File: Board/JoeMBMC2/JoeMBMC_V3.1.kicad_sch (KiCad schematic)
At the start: 69 parts, among them J1 5007620481, J2 CAN2_T, J3 CAN1_T, Q1 BSO615NG, Q2 BSO615NG, Q3 P-Chanel Mosfet, U1 Teensy4.0, U2 SN65HVD230, U3 DCDC 5V, U4 IS281-4, U5 SN65HVD230, U6 DCDC 3.3V, U7 Level Shifter 5V to 3V, U8 Level Shifter 5V to 3V

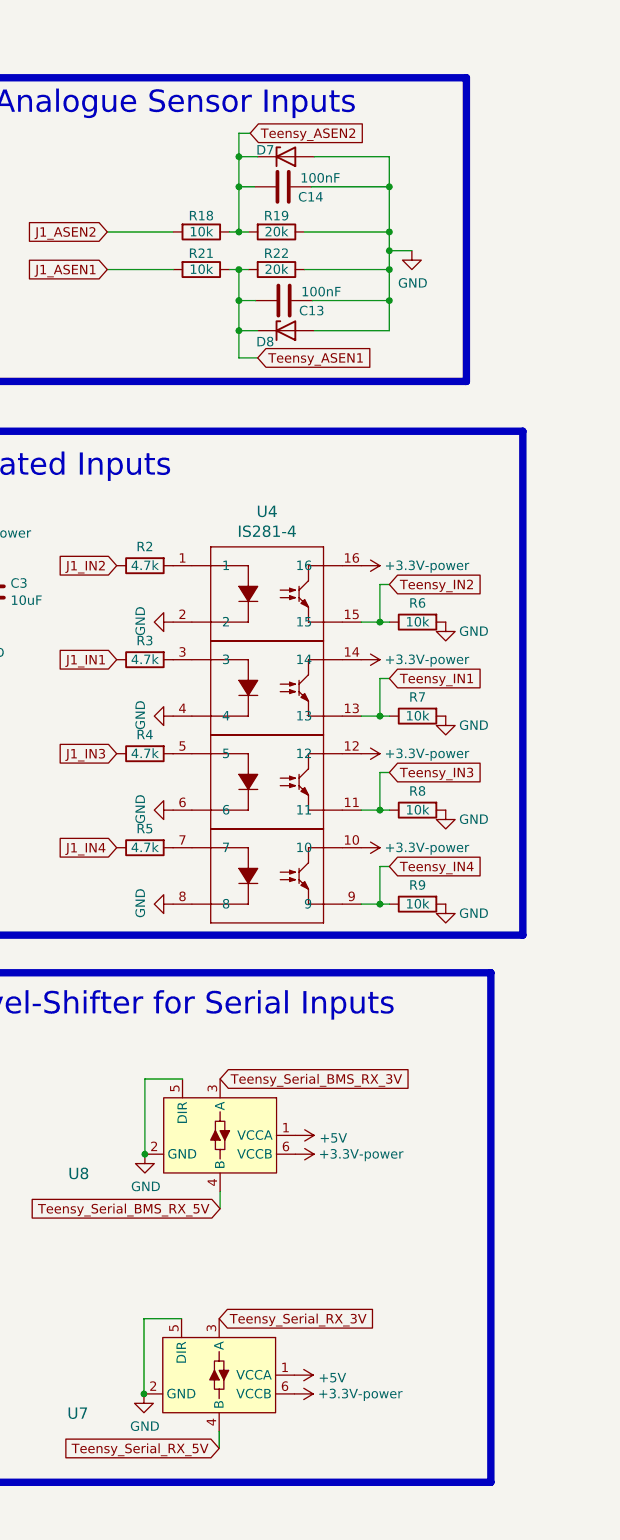
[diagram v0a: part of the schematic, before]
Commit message: remove zener on analogue sensor inputs
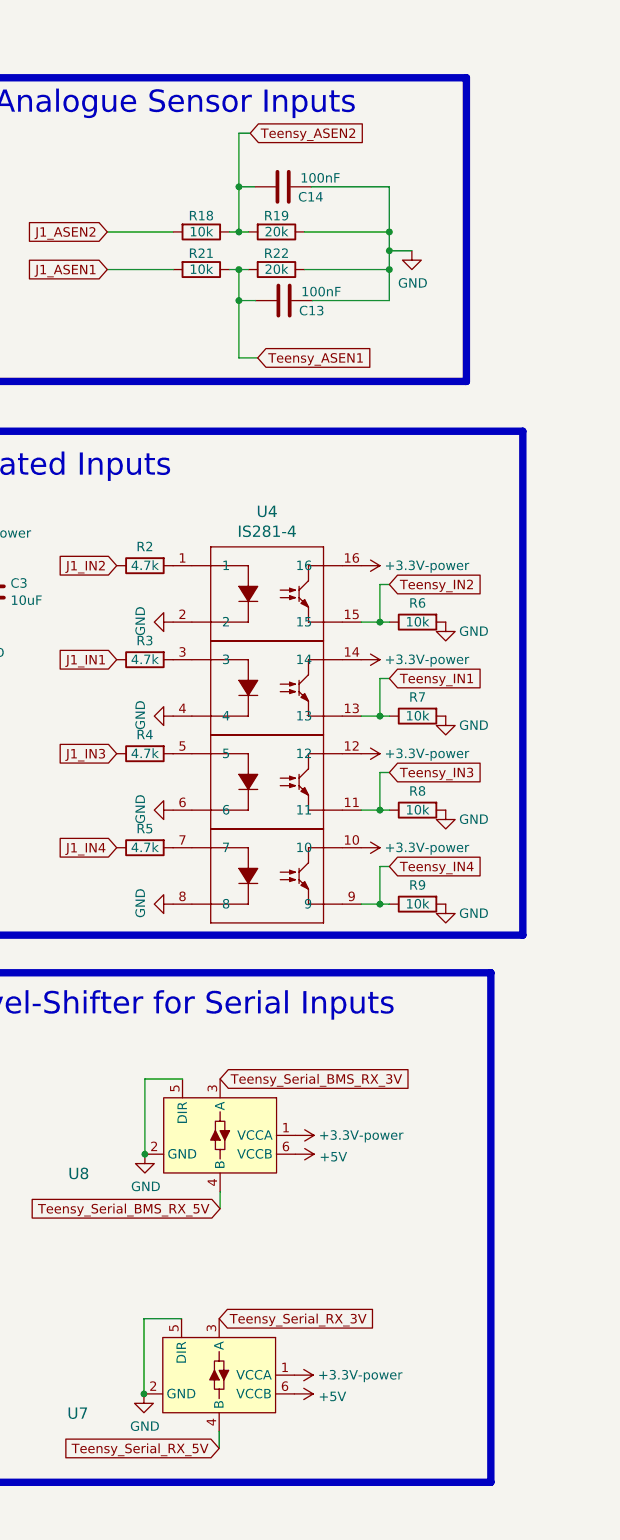
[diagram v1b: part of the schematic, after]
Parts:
- removed D7, D8: D_Zener, Diode_SMD:D_SOD-123, symbol Device:D_Zener
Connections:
- net +3V3: now also U7.1 (VCCA), U8.1 (VCCA); no longer U7.6 (VCCB), U8.6 (VCCB)
- net +5V: now also U7.6 (VCCB), U8.6 (VCCB); no longer U7.1 (VCCA), U8.1 (VCCA)
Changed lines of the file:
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@@
   (junction (at 51.562 69.85) (diameter 0) (color 0 0 0 0)
   )
-  (junction (at 376.301 87.122) (diameter 0) (color 0 0 0 0)
-  )
   (junction (at 355.981 82.931) (diameter 0) (color 0 0 0 0)
   )
@@
   (junction (at 343.154 234.823) (diameter 0) (color 0 0 0 0)
   )
-  (junction (at 355.981 91.186) (diameter 0) (color 0 0 0 0)
-  )
   (junction (at 224.79 253.238) (diameter 0) (color 0 0 0 0)
   )
@@
   (junction (at 68.072 40.64) (diameter 0) (color 0 0 0 0)
   )
-  (junction (at 376.301 71.755) (diameter 0) (color 0 0 0 0)
-  )
   (junction (at 376.301 80.391) (diameter 0) (color 0 0 0 0)
   )
@@
   (junction (at 375.031 143.256) (diameter 0) (color 0 0 0 0)
   )
-  (junction (at 355.981 67.691) (diameter 0) (color 0 0 0 0)
-  )
   (junction (at 81.153 137.16) (diameter 0) (color 0 0 0 0)
   )
@@
     (stroke (width 0) (type default))
   )
-  (wire (pts (xy 355.981 67.691) (xy 358.521 67.691))
-    (stroke (width 0) (type default))
-  )
   (wire (pts (xy 188.341 205.867) (xy 188.849 205.867))
     (stroke (width 0) (type default))
@@
     (stroke (width 0) (type default))
   )
-  (wire (pts (xy 355.981 91.186) (xy 358.521 91.186))
-    (stroke (width 0) (type default))
-  )
   (wire (pts (xy 59.563 144.78) (xy 60.833 144.78))
     (stroke (width 0) (type default))
@@
     (stroke (width 0) (type default))
   )
-  (wire (pts (xy 355.981 87.122) (xy 355.981 91.186))
-    (stroke (width 0) (type default))
-  )
   (wire (pts (xy 68.072 52.07) (xy 68.072 55.88))
     (stroke (width 0) (type default))
   )
-  (wire (pts (xy 376.301 87.122) (xy 376.301 91.186))
-    (stroke (width 0) (type default))
-  )
   (wire (pts (xy 234.95 263.398) (xy 247.65 263.398))
     (stroke (width 0) (type default))
@@
     (stroke (width 0) (type default))
   )
-  (wire (pts (xy 366.141 67.691) (xy 376.301 67.691))
-    (stroke (width 0) (type default))
-  )
   (wire (pts (xy 60.833 137.16) (xy 58.293 137.16))
     (stroke (width 0) (type default))
@@
     (stroke (width 0) (type default))
   )
-  (wire (pts (xy 376.301 67.691) (xy 376.301 71.755))
-    (stroke (width 0) (type default))
-  )
   (wire (pts (xy 50.292 69.85) (xy 51.562 69.85))
     (stroke (width 0) (type default))
@@
     (stroke (width 0) (type default))
   )
-  (wire (pts (xy 355.981 67.691) (xy 355.981 64.516))
-    (stroke (width 0) (type default))
-  )
   (wire (pts (xy 365.76 71.755) (xy 376.301 71.755))
     (stroke (width 0) (type default))
@@
     (stroke (width 0) (type default))
   )
-  (wire (pts (xy 366.141 91.186) (xy 376.301 91.186))
-    (stroke (width 0) (type default))
-  )
   (wire (pts (xy 248.92 206.375) (xy 246.38 206.375))
     (stroke (width 0) (type default))
@@
     (stroke (width 0) (type default))
   )
-  (wire (pts (xy 355.981 91.186) (xy 355.981 94.869))
+  (wire (pts (xy 355.981 87.122) (xy 355.981 94.869))
     (stroke (width 0) (type default))
   )
@@
     (stroke (width 0) (type default))
   )
-  (wire (pts (xy 355.981 67.691) (xy 355.981 71.755))
+  (wire (pts (xy 355.981 64.516) (xy 355.981 71.755))
     (stroke (width 0) (type default))
   )
@@
     )
   )
-  (symbol (lib_id "Device:D_Zener") (at 362.331 91.186 0) (unit 1)
-    (in_bom yes) (on_board yes) (dnp no)
-    (property "Reference" "D8" (at 359.537 92.71 0)
-      (effects (font (size 1.27 1.27)))
-    )
-    (property "Value" "D_Zener" (at 367.665 92.583 0)
-      (effects (font (size 1.27 1.27)) hide)
-    )
-    (property "Footprint" "Diode_SMD:D_SOD-123" (at 362.331 91.186 0)
-      (effects (font (size 1.27 1.27)) hide)
-    )
-    (property "Datasheet" "~" (at 362.331 91.186 0)
-      (effects (font (size 1.27 1.27)) hide)
-    )
-    (property "LCSC" "C2891770" (at 362.331 91.186 0)
-      (effects (font (size 1.27 1.27)) hide)
-    )
-    (pin "2")
-    (pin "1")
-    (instances
-      (project "JoeMBMC_V3.1"
-        (path "/8ca989a6-8473-46db-aafb-d17085f293f9"
-          (reference "D8") (unit 1)
-        )
-      )
-    )
-  )
   (symbol (lib_id "Connector:Conn_01x02_Pin") (at 210.82 201.295 0) (unit 1)
     (in_bom yes) (on_board yes) (dnp no)
@@
     )
   )
-  (symbol (lib_id "Device:D_Zener") (at 362.331 67.691 0) (unit 1)
-    (in_bom yes) (on_board yes) (dnp no)
-    (property "Reference" "D7" (at 359.537 66.802 0)
-      (effects (font (size 1.27 1.27)))
-    )
-    (property "Value" "D_Zener" (at 367.665 69.088 0)
-      (effects (font (size 1.27 1.27)) hide)
-    )
-    (property "Footprint" "Diode_SMD:D_SOD-123" (at 362.331 67.691 0)
-      (effects (font (size 1.27 1.27)) hide)
-    )
-    (property "Datasheet" "~" (at 362.331 67.691 0)
-      (effects (font (size 1.27 1.27)) hide)
-    )
-    (property "LCSC" "C2891770" (at 362.331 67.691 0)
-      (effects (font (size 1.27 1.27)) hide)
-    )
-    (pin "2")
-    (pin "1")
-    (instances
-      (project "JoeMBMC_V3.1"
-        (path "/8ca989a6-8473-46db-aafb-d17085f293f9"
-          (reference "D7") (unit 1)
-        )
-      )
-    )
-  )
   (symbol (lib_id "power:GND") (at 275.463 44.069 0) (unit 1)
     (in_bom yes) (on_board yes) (dnp no)
@@
     )
   )
-  (symbol (lib_id "power:+5V") (at 363.474 232.283 270) (unit 1)
+  (symbol (lib_id "power:+5V") (at 363.474 234.823 270) (unit 1)
     (in_bom yes) (on_board yes) (dnp no)
-    (property "Reference" "#PWR028" (at 359.664 232.283 0)
+    (property "Reference" "#PWR028" (at 359.664 234.823 0)
       (effects (font (size 1.27 1.27)) hide)
     )
-    (property "Value" "+5V" (at 366.7252 232.664 90)
+    (property "Value" "+5V" (at 366.7252 235.204 90)
       (effects (font (size 1.27 1.27)) (justify left))
     )
-    (property "Footprint" "" (at 363.474 232.283 0)
+    (property "Footprint" "" (at 363.474 234.823 0)
       (effects (font (size 1.27 1.27)) hide)
     )
-    (property "Datasheet" "" (at 363.474 232.283 0)
+    (property "Datasheet" "" (at 363.474 234.823 0)
       (effects (font (size 1.27 1.27)) hide)
     )
@@
     )
   )
-  (symbol (lib_id "JoeMBMS_V2.0-rescue:+3.3V-power") (at 363.474 234.823 270) (unit 1)
+  (symbol (lib_id "JoeMBMS_V2.0-rescue:+3.3V-power") (at 363.474 232.283 270) (unit 1)
     (in_bom yes) (on_board yes) (dnp no)
-    (property "Reference" "#PWR029" (at 359.664 234.823 0)
+    (property "Reference" "#PWR029" (at 359.664 232.283 0)
       (effects (font (size 1.27 1.27)) hide)
     )
-    (property "Value" "+3.3V-power" (at 366.6489 234.823 90)
+    (property "Value" "+3.3V-power" (at 366.6489 232.283 90)
       (effects (font (size 1.27 1.27)) (justify left))
     )
-    (property "Footprint" "" (at 363.474 234.823 0)
+    (property "Footprint" "" (at 363.474 232.283 0)
       (effects (font (size 1.27 1.27)) hide)
     )
-    (property "Datasheet" "" (at 363.474 234.823 0)
+    (property "Datasheet" "" (at 363.474 232.283 0)
       (effects (font (size 1.27 1.27)) hide)
     )
@@
     )
   )
-  (symbol (lib_id "power:+5V") (at 363.601 199.898 270) (unit 1)
+  (symbol (lib_id "power:+5V") (at 363.601 202.438 270) (unit 1)
     (in_bom yes) (on_board yes) (dnp no)
-    (property "Reference" "#PWR034" (at 359.791 199.898 0)
+    (property "Reference" "#PWR034" (at 359.791 202.438 0)
       (effects (font (size 1.27 1.27)) hide)
     )
-    (property "Value" "+5V" (at 366.8522 200.279 90)
+    (property "Value" "+5V" (at 366.8522 202.819 90)
       (effects (font (size 1.27 1.27)) (justify left))
     )
-    (property "Footprint" "" (at 363.601 199.898 0)
+    (property "Footprint" "" (at 363.601 202.438 0)
       (effects (font (size 1.27 1.27)) hide)
     )
-    (property "Datasheet" "" (at 363.601 199.898 0)
+    (property "Datasheet" "" (at 363.601 202.438 0)
       (effects (font (size 1.27 1.27)) hide)
     )
@@
     )
   )
-  (symbol (lib_id "JoeMBMS_V2.0-rescue:+3.3V-power") (at 363.601 202.438 270) (unit 1)
+  (symbol (lib_id "JoeMBMS_V2.0-rescue:+3.3V-power") (at 363.601 199.898 270) (unit 1)
     (in_bom yes) (on_board yes) (dnp no)
-    (property "Reference" "#PWR035" (at 359.791 202.438 0)
+    (property "Reference" "#PWR035" (at 359.791 199.898 0)
       (effects (font (size 1.27 1.27)) hide)
     )
-    (property "Value" "+3.3V-power" (at 366.7759 202.438 90)
+    (property "Value" "+3.3V-power" (at 366.7759 199.898 90)
       (effects (font (size 1.27 1.27)) (justify left))
     )
-    (property "Footprint" "" (at 363.601 202.438 0)
+    (property "Footprint" "" (at 363.601 199.898 0)
       (effects (font (size 1.27 1.27)) hide)
     )
-    (property "Datasheet" "" (at 363.601 202.438 0)
+    (property "Datasheet" "" (at 363.601 199.898 0)
       (effects (font (size 1.27 1.27)) hide)
     )

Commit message: USB-Flex-Board
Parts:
- D1, D2, D3, D4: LCSC C37049 -> C8598
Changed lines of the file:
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@@
       (effects (font (size 1.27 1.27)) hide)
     )
-    (property "LCSC" "C37049" (at 71.882 91.44 0)
+    (property "LCSC" "C8598" (at 71.882 91.44 0)
       (effects (font (size 1.27 1.27)) hide)
     )
@@
       (effects (font (size 1.27 1.27)) hide)
     )
-    (property "LCSC" "C37049" (at 71.882 80.01 0)
+    (property "LCSC" "C8598" (at 71.882 80.01 0)
       (effects (font (size 1.27 1.27)) hide)
     )
@@
       (effects (font (size 1.27 1.27)) hide)
     )
-    (property "LCSC" "C37049" (at 71.882 52.07 0)
+    (property "LCSC" "C8598" (at 71.882 52.07 0)
       (effects (font (size 1.27 1.27)) hide)
     )
@@
       (effects (font (size 1.27 1.27)) hide)
     )
-    (property "LCSC" "C37049" (at 71.882 40.64 0)
-      (effects (font (size 1.27 1.27)) hide)
-    )
+    (property "LCSC" "C8598" (at 71.882 40.64 0)
+      (effects (font (size 1.27 1.27)) hide)
+    )
